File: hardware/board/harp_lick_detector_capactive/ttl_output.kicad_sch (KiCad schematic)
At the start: 8 parts

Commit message: add driven shield
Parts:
- C?: value (none) -> 10uF; footprint (none) -> Capacitor_SMD:C_0805_2012Metric
- J?: value (none) -> Conn_Coaxial
- R?: value (none) -> 47
- U? (x5): value (none) -> 74HC04
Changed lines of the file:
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@@
     (in_bom yes) (on_board yes)
     (property "Reference" "U?" (id 0) (at 147.32 85.09 0))
-    (property "Value" "" (id 1) (at 147.32 87.63 0))
+    (property "Value" "74HC04" (id 1) (at 147.32 87.63 0))
     (property "Footprint" "" (id 2) (at 144.78 91.44 0)
       (effects (font (size 1.27 1.27)) hide)
@@
       (effects (font (size 1.27 1.27)) (justify left))
     )
-    (property "Value" "" (id 1) (at 173.99 93.0031 0)
+    (property "Value" "Conn_Coaxial" (id 1) (at 173.99 93.0031 0)
       (effects (font (size 1.27 1.27)) (justify left))
     )
@@
     (in_bom yes) (on_board yes)
     (property "Reference" "U?" (id 0) (at 146.05 96.52 0))
-    (property "Value" "" (id 1) (at 147.32 99.06 0))
+    (property "Value" "74HC04" (id 1) (at 147.32 99.06 0))
     (property "Footprint" "" (id 2) (at 144.78 102.87 0)
       (effects (font (size 1.27 1.27)) hide)
@@
     (in_bom yes) (on_board yes)
     (property "Reference" "U?" (id 0) (at 147.32 74.93 0))
-    (property "Value" "" (id 1) (at 147.32 77.47 0))
+    (property "Value" "74HC04" (id 1) (at 147.32 77.47 0))
     (property "Footprint" "" (id 2) (at 144.78 81.28 0)
       (effects (font (size 1.27 1.27)) hide)
@@
       (effects (font (size 1.27 1.27)) (justify left))
     )
-    (property "Value" "" (id 1) (at 46.99 176.53 0)
-      (effects (font (size 1.27 1.27)) (justify left))
-    )
-    (property "Footprint" "" (id 2) (at 46.6852 177.8 0)
+    (property "Value" "10uF" (id 1) (at 46.99 176.53 0)
+      (effects (font (size 1.27 1.27)) (justify left))
+    )
+    (property "Footprint" "Capacitor_SMD:C_0805_2012Metric" (id 2) (at 46.6852 177.8 0)
       (effects (font (size 1.27 1.27)) hide)
     )
@@
       (effects (font (size 1.27 1.27)) (justify left))
     )
-    (property "Value" "" (id 1) (at 30.48 175.2599 0)
+    (property "Value" "74HC04" (id 1) (at 30.48 175.2599 0)
       (effects (font (size 1.27 1.27)) (justify left))
     )
@@
     (in_bom yes) (on_board yes)
     (property "Reference" "R?" (id 0) (at 158.75 88.9 90))
-    (property "Value" "" (id 1) (at 160.02 91.44 90))
+    (property "Value" "47" (id 1) (at 160.02 91.44 90))
     (property "Footprint" "" (id 2) (at 160.02 93.218 90)
       (effects (font (size 1.27 1.27)) hide)
@@
     (in_bom yes) (on_board yes) (fields_autoplaced)
     (property "Reference" "U?" (id 0) (at 125.73 82.55 0))
-    (property "Value" "" (id 1) (at 125.73 85.09 0))
+    (property "Value" "74HC04" (id 1) (at 125.73 85.09 0))
     (property "Footprint" "" (id 2) (at 125.73 91.44 0)
       (effects (font (size 1.27 1.27)) hide)

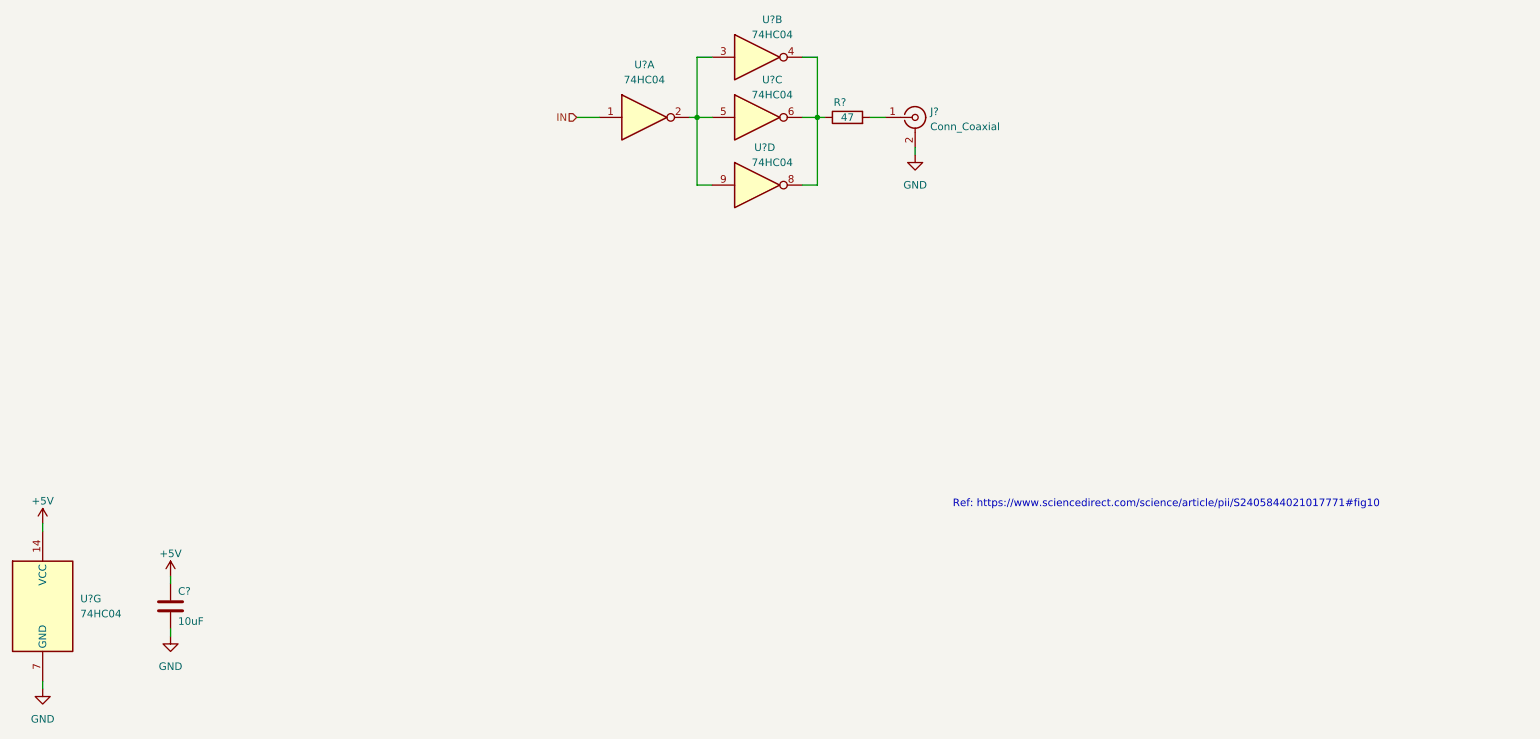
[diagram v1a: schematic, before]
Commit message: add extra series termination resistors
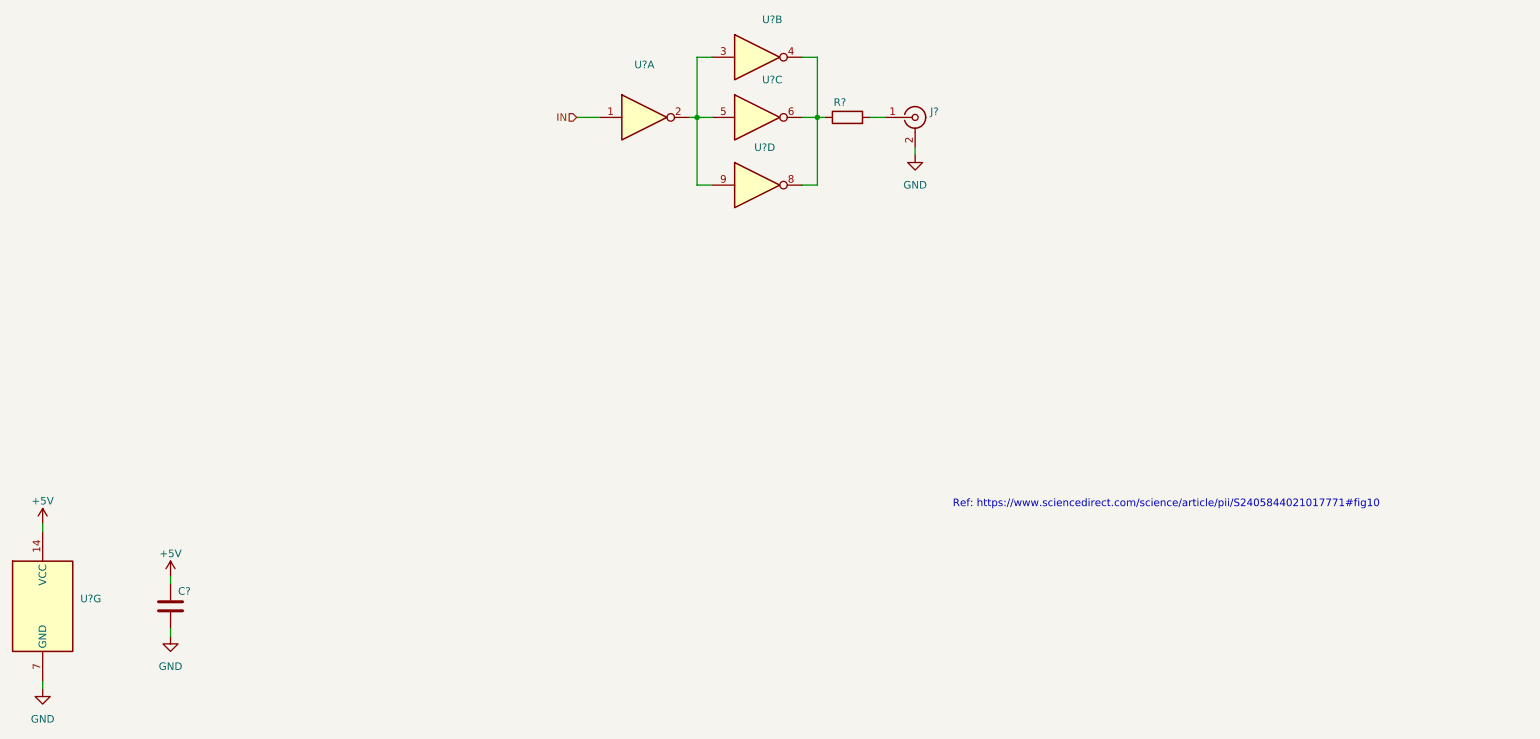
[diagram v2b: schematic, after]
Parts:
- C?: value 10uF -> (none); footprint Capacitor_SMD:C_0805_2012Metric -> (none)
- J?: value Conn_Coaxial -> (none)
- R?: value 47 -> (none)
- U? (x5): value 74HC04 -> (none)
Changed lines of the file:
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@@
     (in_bom yes) (on_board yes)
     (property "Reference" "U?" (id 0) (at 147.32 85.09 0))
-    (property "Value" "74HC04" (id 1) (at 147.32 87.63 0))
+    (property "Value" "" (id 1) (at 147.32 87.63 0))
     (property "Footprint" "" (id 2) (at 144.78 91.44 0)
       (effects (font (size 1.27 1.27)) hide)
@@
       (effects (font (size 1.27 1.27)) (justify left))
     )
-    (property "Value" "Conn_Coaxial" (id 1) (at 173.99 93.0031 0)
+    (property "Value" "" (id 1) (at 173.99 93.0031 0)
       (effects (font (size 1.27 1.27)) (justify left))
     )
@@
     (in_bom yes) (on_board yes)
     (property "Reference" "U?" (id 0) (at 146.05 96.52 0))
-    (property "Value" "74HC04" (id 1) (at 147.32 99.06 0))
+    (property "Value" "" (id 1) (at 147.32 99.06 0))
     (property "Footprint" "" (id 2) (at 144.78 102.87 0)
       (effects (font (size 1.27 1.27)) hide)
@@
     (in_bom yes) (on_board yes)
     (property "Reference" "U?" (id 0) (at 147.32 74.93 0))
-    (property "Value" "74HC04" (id 1) (at 147.32 77.47 0))
+    (property "Value" "" (id 1) (at 147.32 77.47 0))
     (property "Footprint" "" (id 2) (at 144.78 81.28 0)
       (effects (font (size 1.27 1.27)) hide)
@@
       (effects (font (size 1.27 1.27)) (justify left))
     )
-    (property "Value" "10uF" (id 1) (at 46.99 176.53 0)
-      (effects (font (size 1.27 1.27)) (justify left))
-    )
-    (property "Footprint" "Capacitor_SMD:C_0805_2012Metric" (id 2) (at 46.6852 177.8 0)
+    (property "Value" "" (id 1) (at 46.99 176.53 0)
+      (effects (font (size 1.27 1.27)) (justify left))
+    )
+    (property "Footprint" "" (id 2) (at 46.6852 177.8 0)
       (effects (font (size 1.27 1.27)) hide)
     )
@@
       (effects (font (size 1.27 1.27)) (justify left))
     )
-    (property "Value" "74HC04" (id 1) (at 30.48 175.2599 0)
+    (property "Value" "" (id 1) (at 30.48 175.2599 0)
       (effects (font (size 1.27 1.27)) (justify left))
     )
@@
     (in_bom yes) (on_board yes)
     (property "Reference" "R?" (id 0) (at 158.75 88.9 90))
-    (property "Value" "47" (id 1) (at 160.02 91.44 90))
+    (property "Value" "" (id 1) (at 160.02 91.44 90))
     (property "Footprint" "" (id 2) (at 160.02 93.218 90)
       (effects (font (size 1.27 1.27)) hide)
@@
     (in_bom yes) (on_board yes) (fields_autoplaced)
     (property "Reference" "U?" (id 0) (at 125.73 82.55 0))
-    (property "Value" "74HC04" (id 1) (at 125.73 85.09 0))
+    (property "Value" "" (id 1) (at 125.73 85.09 0))
     (property "Footprint" "" (id 2) (at 125.73 91.44 0)
       (effects (font (size 1.27 1.27)) hide)
